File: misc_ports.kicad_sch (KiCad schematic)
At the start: 31 parts, among them J10 Molex 46765-2301, J3 Wuerth_7499010121A, J7 QMTECH JTAG, J8 RTC, J9 1140084168 microSD Card Slot, P1 Full-side CD Card Slot, U12 DP83826, U13 74LVC374, U14 PTN3363BSMP

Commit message: add mezannine for joystick ports to de-clutter board.
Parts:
- J10: footprint Connector_HDMI:HDMI_Micro-D_Molex_46765-2x0x -> Connector_HDMI:HDMI_A_Contact_Technology_HDMI-19APL2_Horizontal
- J9: footprint AMPHENOL_1140084168 -> snapeda:AMPHENOL_1140084168
- P1: footprint YAMAICHI_FPS009-2405-0 -> snapeda:YAMAICHI_FPS009-2405-0
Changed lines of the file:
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@@
     (property "Reference" "J9" (id 0) (at 217.17 36.83 0))
     (property "Value" "1140084168 microSD Card Slot" (id 1) (at 217.17 39.37 0))
-    (property "Footprint" "AMPHENOL_1140084168" (id 2) (at 203.2 45.72 0)
+    (property "Footprint" "snapeda:AMPHENOL_1140084168" (id 2) (at 203.2 45.72 0)
       (effects (font (size 1.27 1.27)) (justify left bottom) hide)
     )
@@
       (effects (font (size 1.27 1.27)) (justify left))
     )
-    (property "Footprint" "Connector_HDMI:HDMI_Micro-D_Molex_46765-2x0x" (id 2) (at 269.875 119.38 0)
+    (property "Footprint" "Connector_HDMI:HDMI_A_Contact_Technology_HDMI-19APL2_Horizontal" (id 2) (at 269.875 119.38 0)
       (effects (font (size 1.27 1.27)) hide)
     )
@@
     (property "Reference" "P1" (id 0) (at 139.7 19.05 0))
     (property "Value" "Full-side CD Card Slot" (id 1) (at 139.7 21.59 0))
-    (property "Footprint" "YAMAICHI_FPS009-2405-0" (id 2) (at 139.7 41.91 0)
+    (property "Footprint" "snapeda:YAMAICHI_FPS009-2405-0" (id 2) (at 139.7 41.91 0)
       (effects (font (size 1.27 1.27)) (justify left bottom) hide)
     )

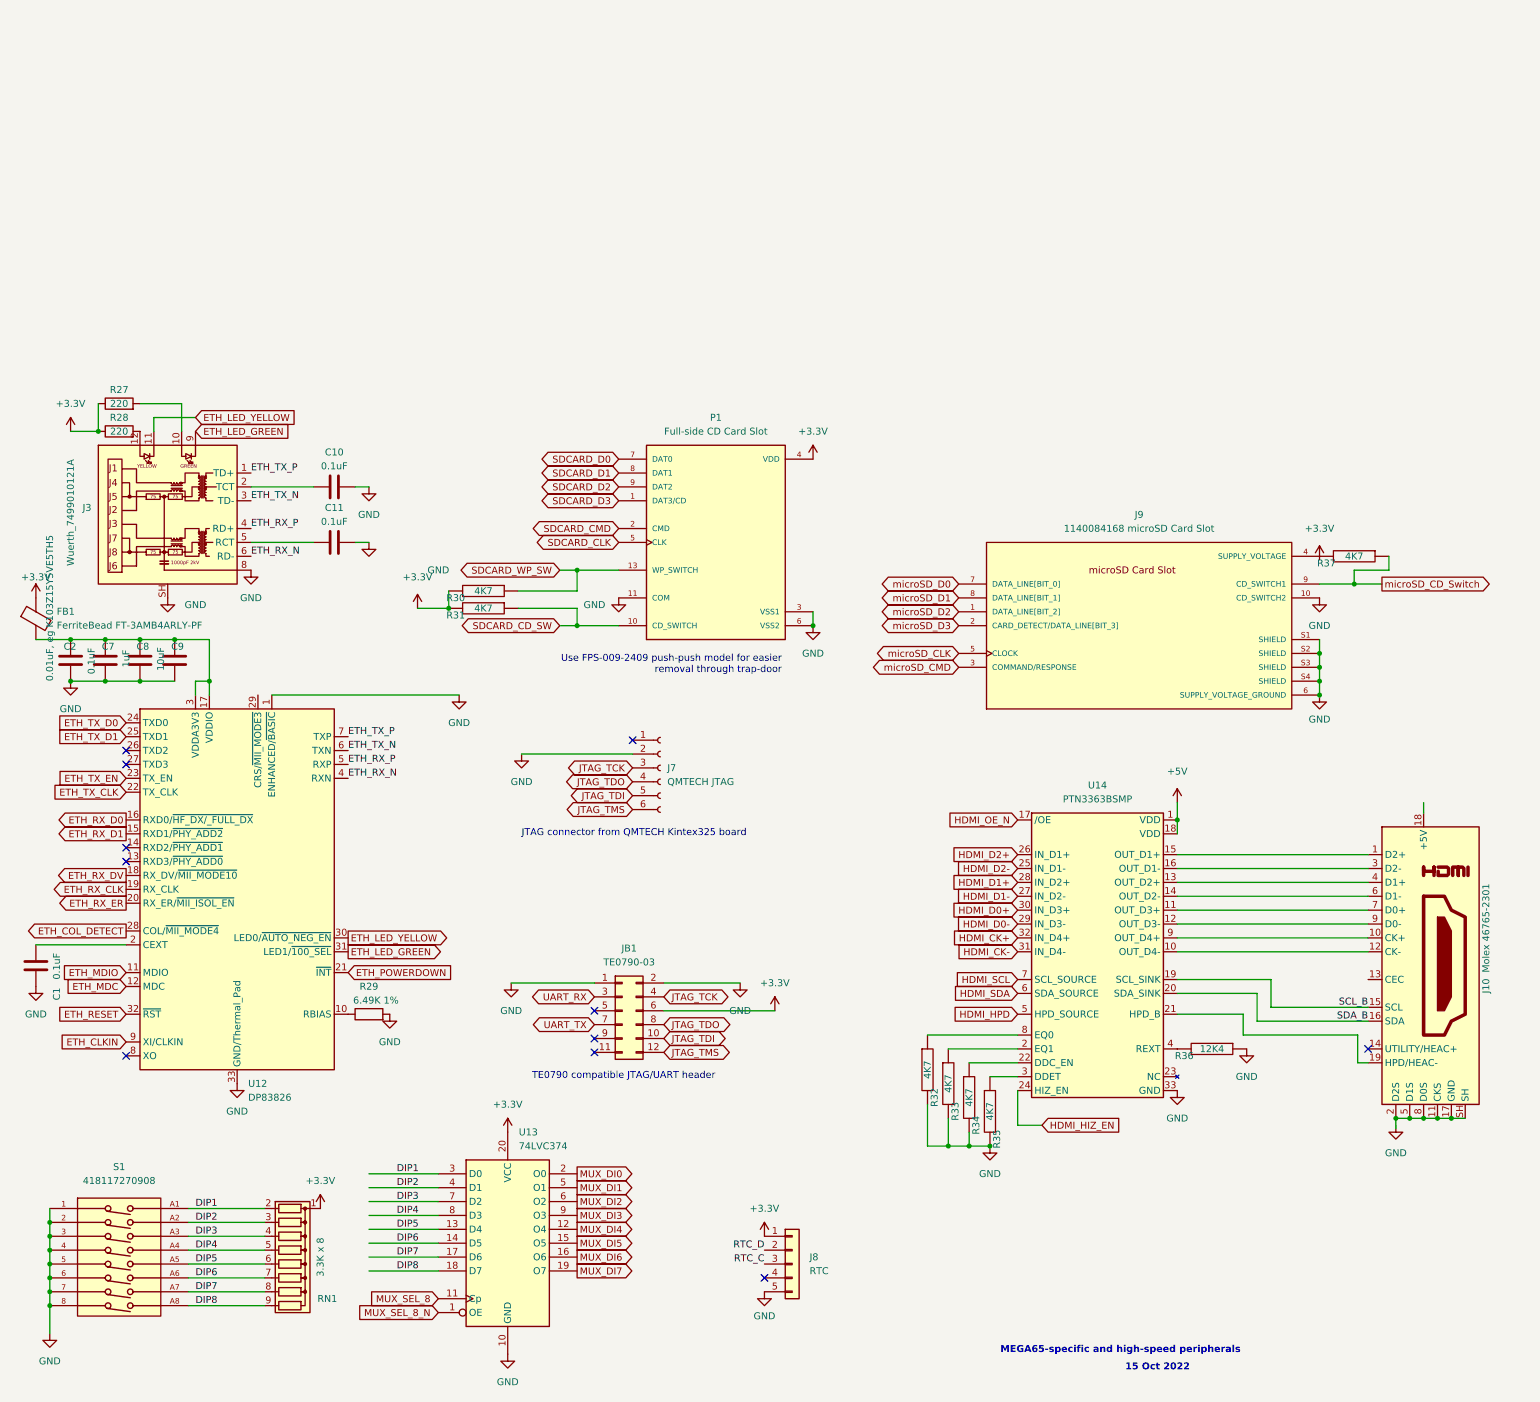
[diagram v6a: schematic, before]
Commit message: add missing MEGA65 keyboard connector and keyboard JTAG header #10 #12
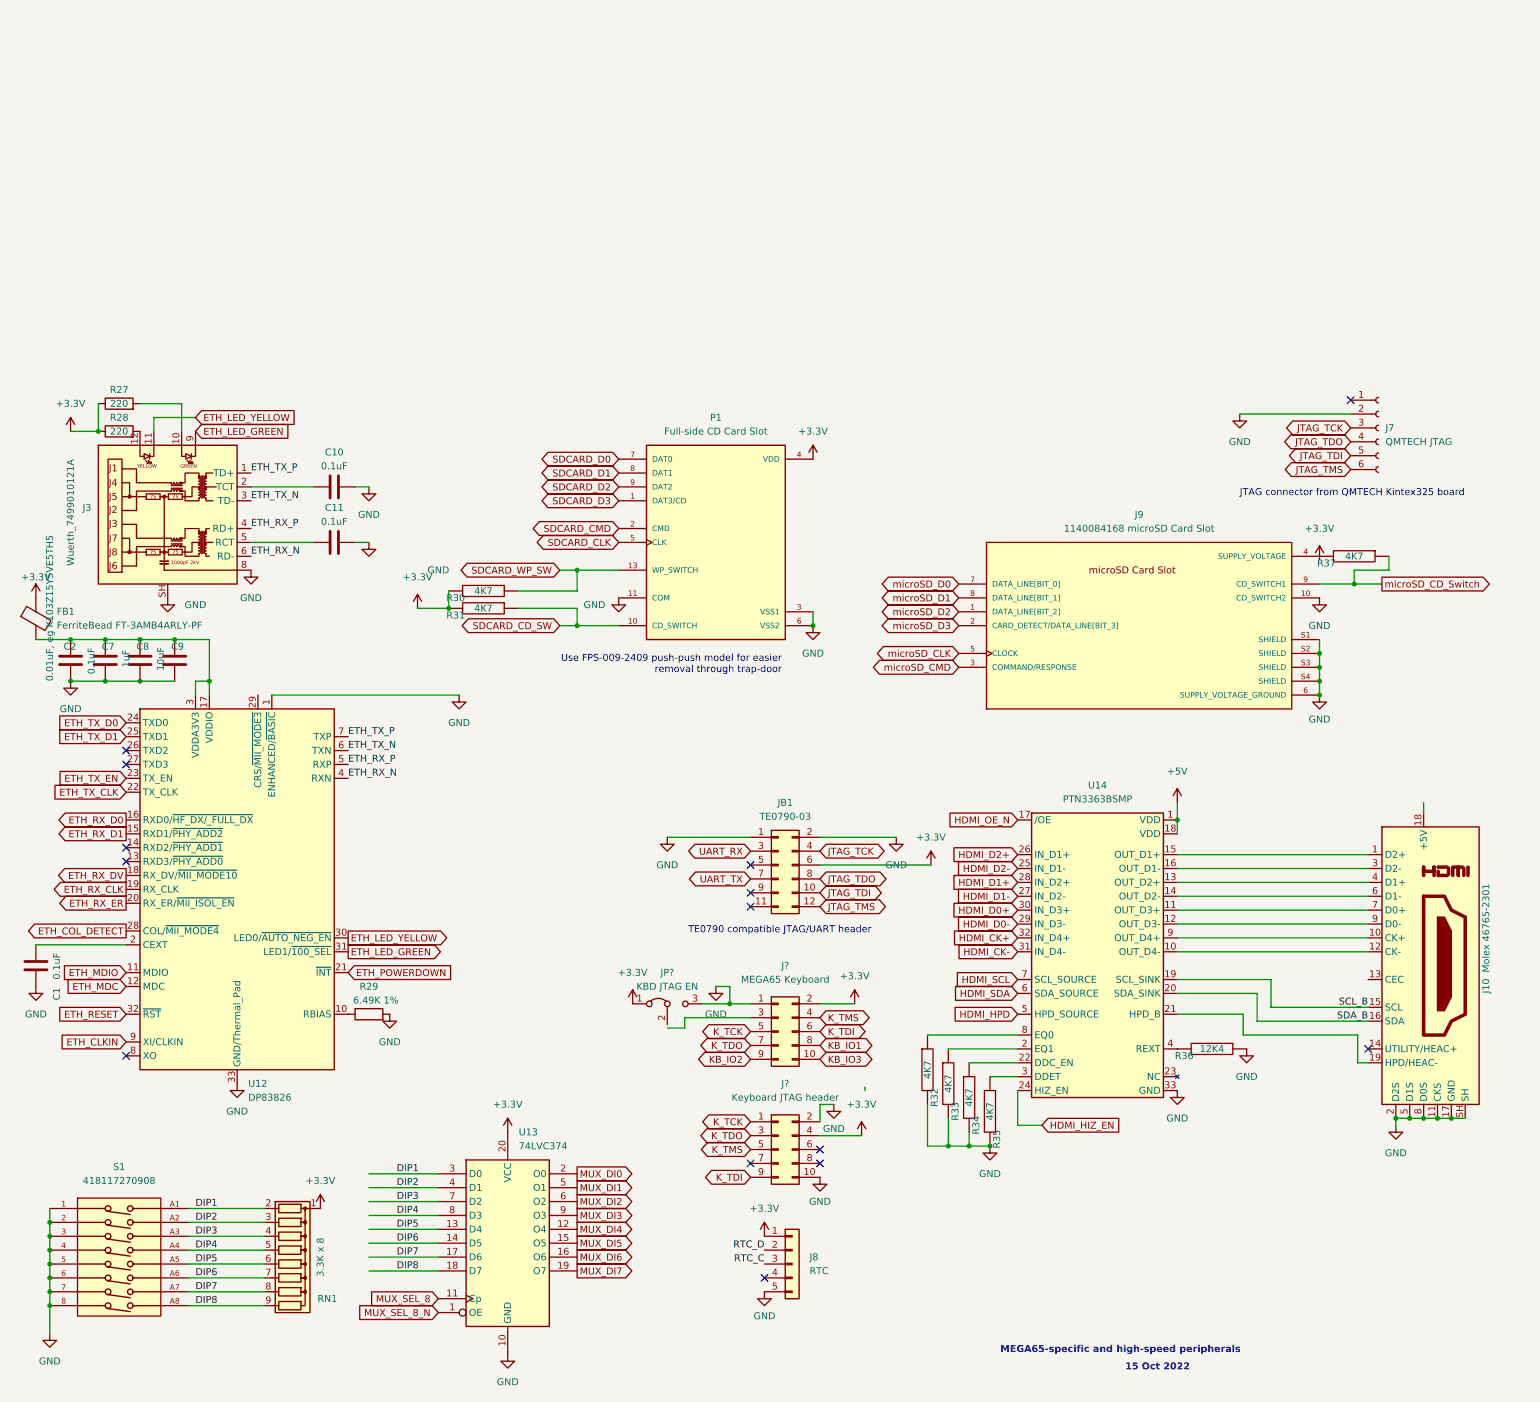
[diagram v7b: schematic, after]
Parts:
- added J?: Keyboard JTAG header, Connector_PinHeader_2.54mm:PinHeader_2x05_P2.54mm_Vertical, symbol Connector_Generic:Conn_02x05_Odd_Even
- added J?: MEGA65 Keyboard, symbol Connector_Generic:Conn_02x05_Odd_Even
- added JP?: KBD JTAG EN, Connector_PinHeader_2.54mm:PinHeader_1x03_P2.54mm_Vertical, symbol Jumper:Jumper_3_Bridged12
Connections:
- net +3V3: now also J?.2 (Pin_2), J?.4 (Pin_4), JP?.1 (A)
- net GND: now also J?.1 (Pin_1), J?.10 (Pin_10), J?.2 (Pin_2), JP?.3 (B)
- new net KB_IO1: J?.8 (Pin_8)
- new net KB_IO2: J?.9 (Pin_9)
- new net KB_IO3: J?.10 (Pin_10)
- new net K_TCK: J?.1 (Pin_1), J?.5 (Pin_5)
- new net K_TDI: J?.6 (Pin_6), J?.9 (Pin_9)
- new net K_TDO: J?.3 (Pin_3), J?.7 (Pin_7)
- new net K_TMS: J?.4 (Pin_4), J?.5 (Pin_5)
- no-connect marks 11 -> 14
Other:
- moved on the sheet: J7, JB1
